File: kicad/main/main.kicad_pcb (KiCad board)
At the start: 2 copper layers, 45.7 x 35 mm, 19 parts, among them J2 Conn_01x02, J3 Conn_01x07_Pin, J4 Conn_01x04_Pin, P1 USB_C_Plug_USB2.0, SW1 MK-12C03-G015, SW3 SW_Push, SW4 SW_Push, U1 HUSB237, U2 ZX-PH2.0-WT4P

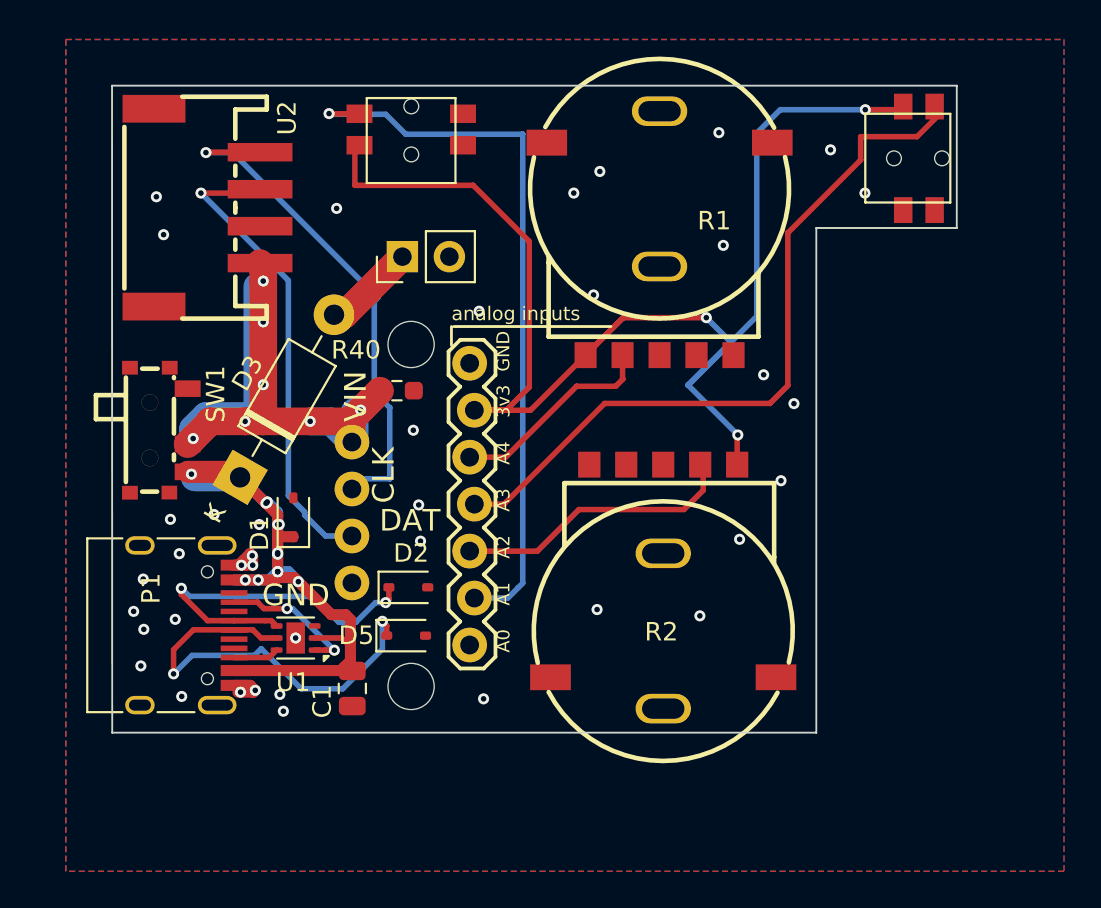
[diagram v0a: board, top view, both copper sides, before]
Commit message: Final push with moved components
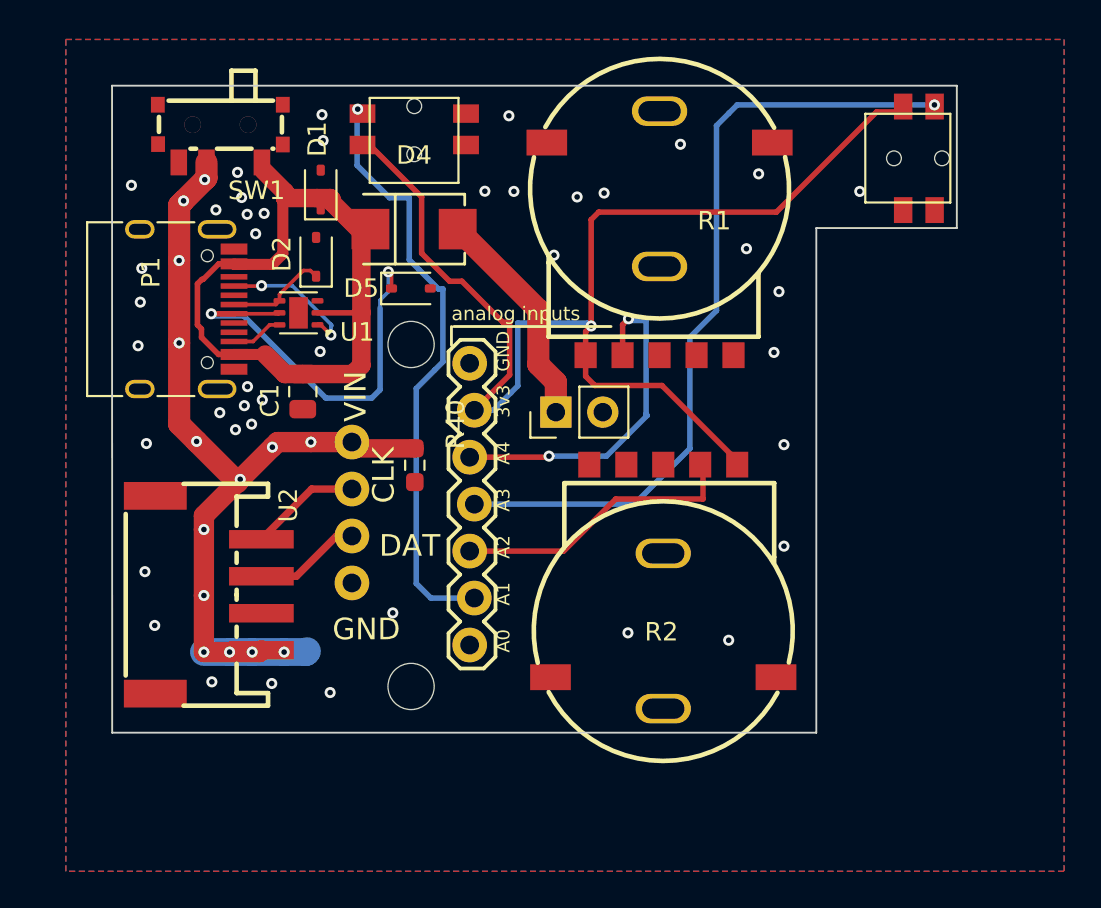
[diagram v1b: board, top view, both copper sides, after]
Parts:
- removed D3: 1N4007, Diode_THT:D_DO-41_SOD81_P10.16mm_Horizontal
- added D4: SK44BL-TP, easyeda2kicad:SMB_L4.6-W3.6-LS5.3-RD, F.Cu at (176.3, 82.8)
- moved U2 20.9 mm to (165.2, 102.5)
- moved D5 18.8 mm to (176.2, 86.0)
- moved D2 18.6 mm to (171.0, 84.3), turned to 90 degrees
- moved D1 17.8 mm to (171.3, 80.6)
- moved U1 17.6 mm to (170.1, 87.3)
- moved P1 17.1 mm to (162.6, 87.1)
- moved SW1 16.4 mm to (165.9, 77.6), turned to 180 degrees
- moved C1 16.3 mm to (170.3, 91.5)
- moved J2 11.8 mm to (184.0, 92.7)
- moved R40 4.15 mm to (176.4, 95.5), turned to 90 degrees
- moved SW3 0.16 mm to (176.3, 77.4)
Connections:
- SW1 pad 1: unconnected-(SW1-Pad1) -> VBUS
- SW1 pad 3: VBUS -> unconnected-(SW1-Pad3)
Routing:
- net VIN: track 37.9 -> 84.9 mm, vias 7 -> 14
- net SCK_OUT: track 28.0 -> 6.02 mm, vias 1 -> 0
- net MOSI_OUT: track 26.1 -> 5.80 mm, vias 1 -> 0
- net D+: track 19.4 -> 5.54 mm, vias 2 -> 0
- net +3V3: track 76.3 -> 67.9 mm, vias 3 -> 1
- net AIN4: track 11.3 -> 18.8 mm, vias 0 -> 2
- net AIN1: track 39.9 -> 32.4 mm
- net Net-(D4-A): track 5.00 -> 12.1 mm
- net GND: track 4.82 -> 0.00 mm, vias 39 -> 42
- net AIN3: track 39.8 -> 43.4 mm, vias 0 -> 1
- net VBUS: track 40.5 -> 38.3 mm, vias 12 -> 0
- net D-: track 23.6 -> 22.5 mm
- net CC1: track 7.58 -> 8.23 mm

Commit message: Revamped PCB
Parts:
- removed R2: RK10J11R0A0H, easyeda2kicad:RES-SMD_RK10J11R0A0H
- removed SW1: MK-12C03-G015, easyeda2kicad:SW-SMD_MK-12C03-G015
- removed U2: ZX-PH2.0-WT4P, easyeda2kicad:CONN-SMD_4P-P2.00_C2001RS10411M0101RC
- added J9: Conn_01x02, 1X08_LOCK_513, F.Cu at (203.7, 104.0)
- added SW2: MK-12D18-G040, easyeda2kicad:SW-TH_MK-12D18-G040, F.Cu at (164.7, 77.1)
- added U3: S4B-XH-SM4-TB-(LF)(SN), easyeda2kicad:CONN-SMD_S4B-XH-SM4-TB-LF-SN, F.Cu at (163.3, 101.9)
- moved P1 2.66 mm to (159.9, 87.3)
- moved SW4 2.54 mm to (201.7, 77.2), turned to 180 degrees
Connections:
- J3 pad 2: AIN1 -> AIN2
- J3 pad 3: AIN2 -> AIN1
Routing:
- net VIN: track 84.9 -> 115.2 mm, vias 14 -> 21
- net AIN1: track 32.4 -> 60.2 mm, vias 1 -> 2
- net GND: track 0.00 -> 23.3 mm, vias 42 -> 54
- net VBUS: track 38.3 -> 57.6 mm, vias 0 -> 9
- net AIN2: track 15.7 -> 0.00 mm
- net +3V3: track 67.9 -> 53.3 mm
- net SCK_OUT: track 6.02 -> 15.3 mm, vias 0 -> 1
- net AIN4: track 18.8 -> 15.5 mm
- net CC1: track 8.23 -> 11.1 mm
- net D+: track 5.54 -> 8.30 mm
- net CC2: track 2.83 -> 5.55 mm
- net AIN3: track 43.4 -> 45.5 mm
- net D-: track 22.5 -> 24.0 mm
- net MOSI_OUT: track 5.80 -> 4.88 mm
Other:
- board size 45.7 x 35 mm -> 48.3 x 35 mm
- board text added: "IO25"
- board text added: "IO26"
